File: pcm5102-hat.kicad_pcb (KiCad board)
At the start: 2 copper layers, 46.7 x 51.8 mm, 2 parts, among them J1 GPIO

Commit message: finish routing
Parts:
- moved U1 1.00 mm to (90.6, 95.5)
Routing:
- net +5V: track 0.00 -> 74.8 mm
- net BCK: track 0.00 -> 58.5 mm
- net DIN: track 0.00 -> 47.9 mm
- net LCK: track 0.00 -> 42.9 mm
- net GND: vias 0 -> 1
- added copper zone on B.Cu, net GND
- added copper zone on F.Cu, net GND
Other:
- board size 46.7 x 51.8 mm -> 48 x 51.8 mm

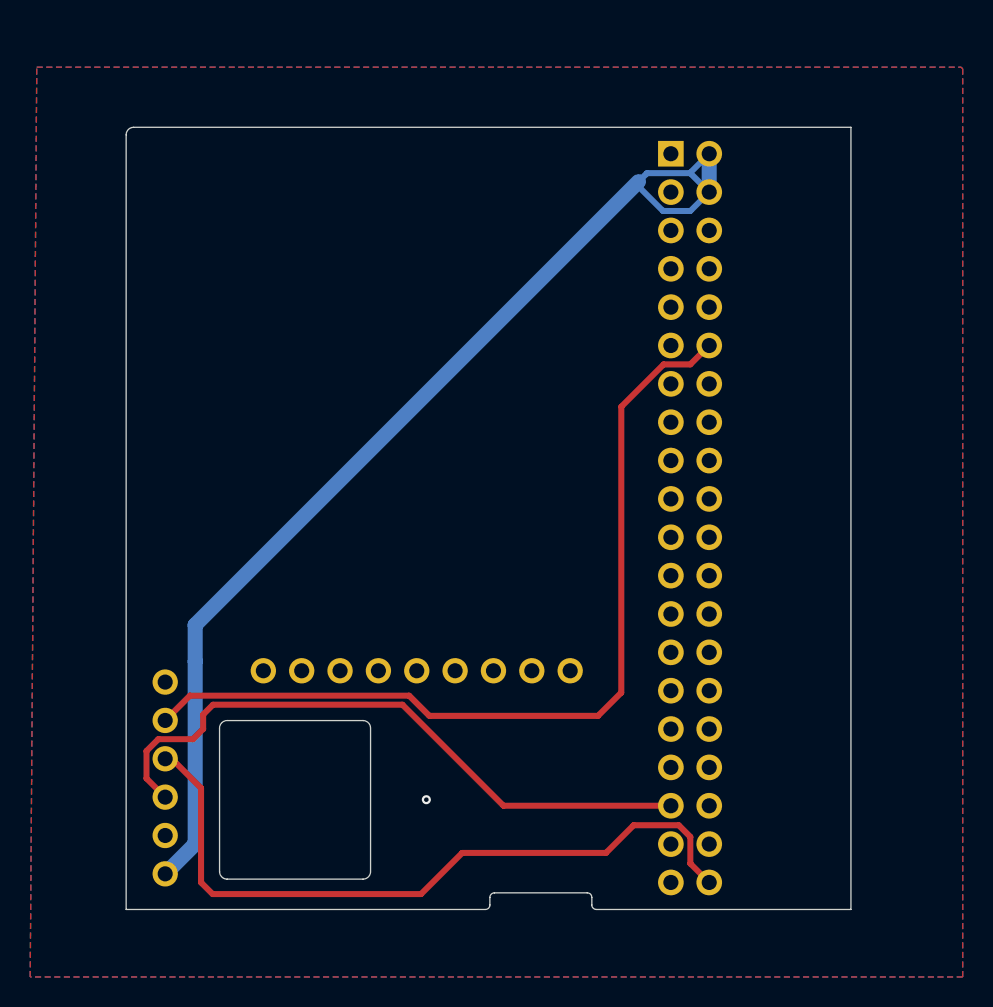
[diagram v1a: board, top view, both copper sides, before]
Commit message: fix some DRC errors
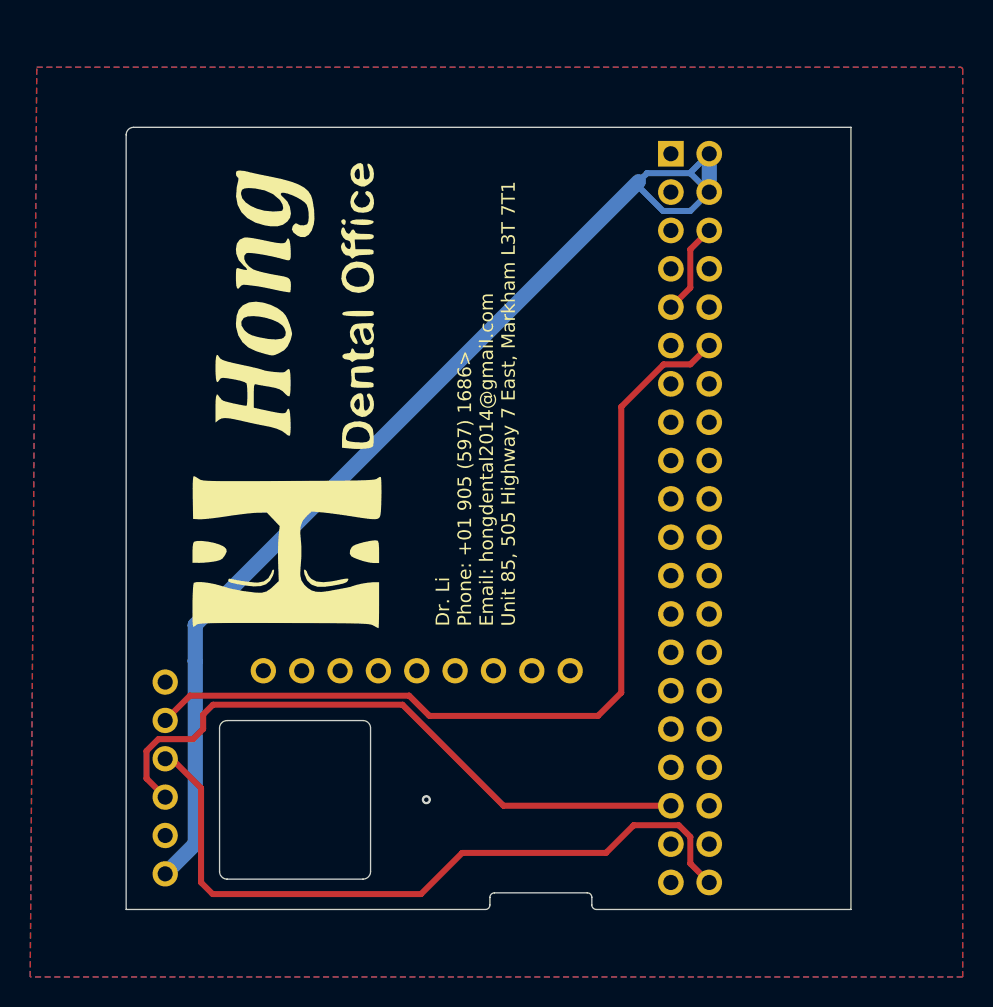
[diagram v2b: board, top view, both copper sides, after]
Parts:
- added G***: LOGO, LOGO, F.Cu at (100.4, 78.9)
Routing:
- net GND: track 0.00 -> 6.13 mm
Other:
- board text added: "Dr. Li Phone: +01 905 (597) 1686> Email: hongdental2014@gmail.com Unit 85, 505 Highway 7 East, Markham L3T 7T1"
